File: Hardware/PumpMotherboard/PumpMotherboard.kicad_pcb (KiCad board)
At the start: 2 copper layers, 86.4 x 91.4 mm, 0 parts

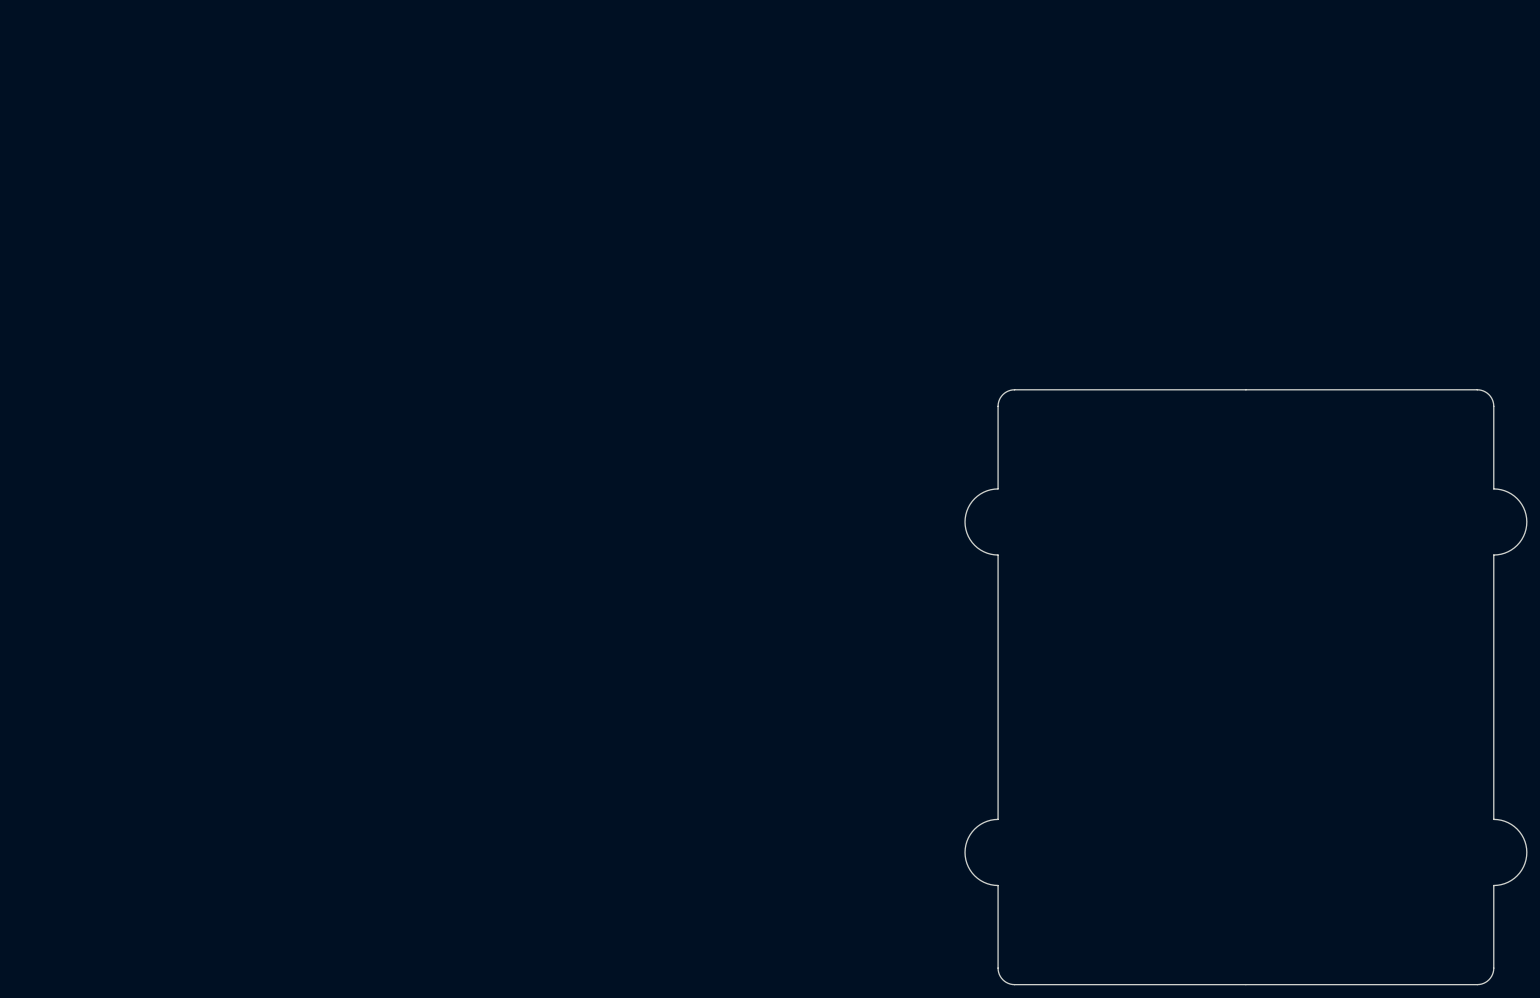
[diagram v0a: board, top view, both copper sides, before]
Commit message: Add more bits to motherboard/controller panel
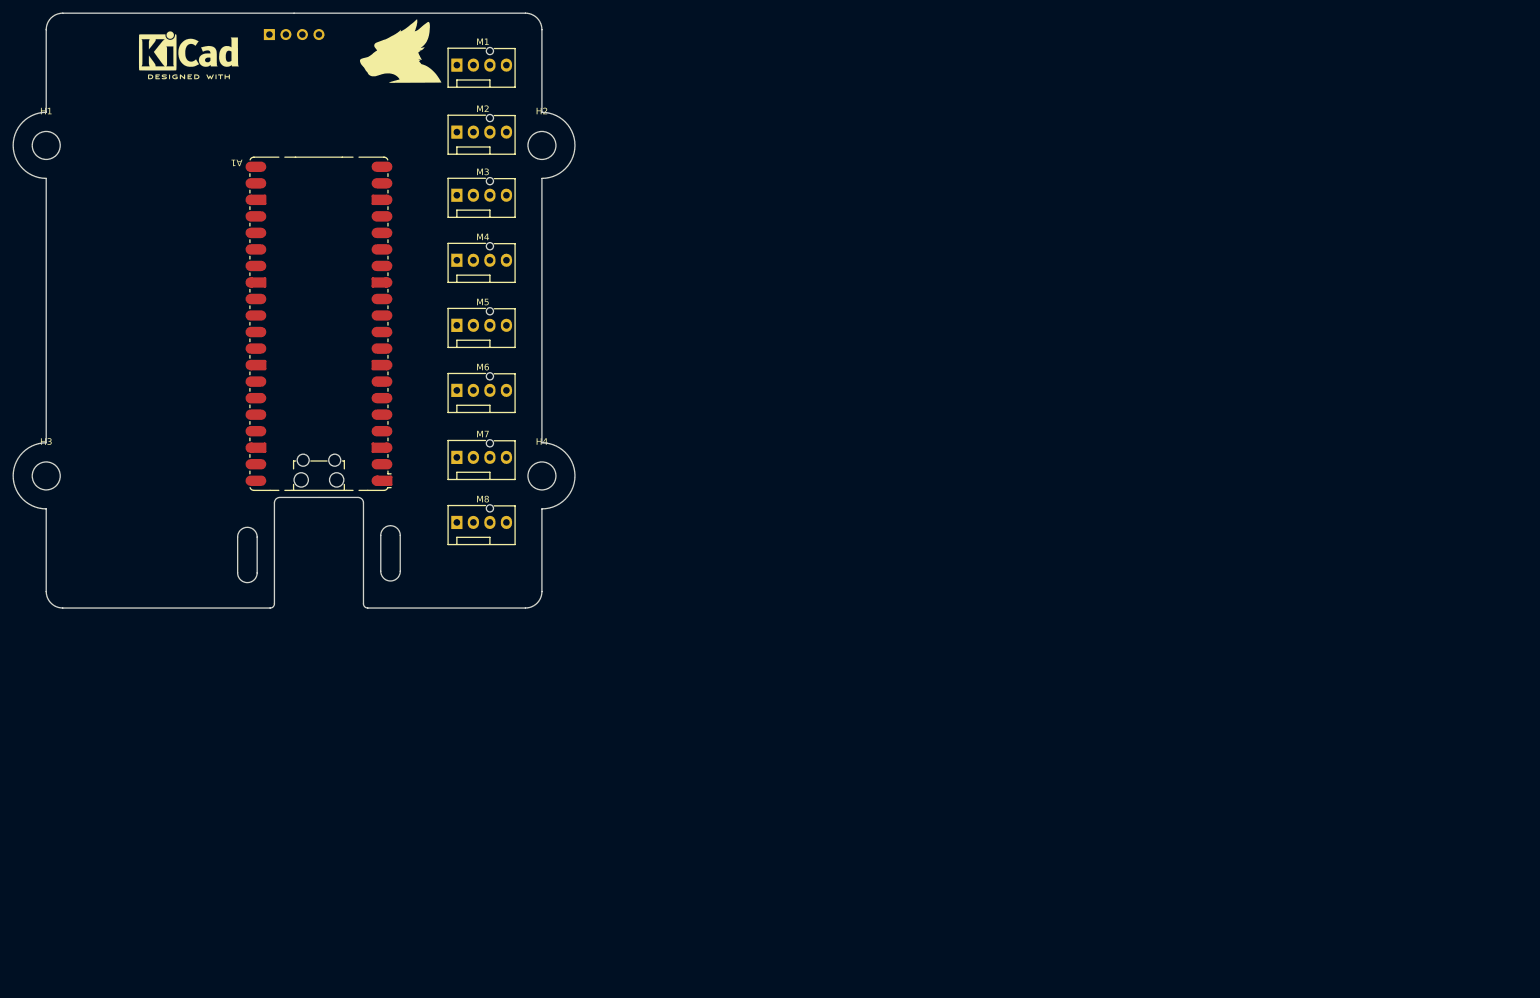
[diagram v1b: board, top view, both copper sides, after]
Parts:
- added A1: RaspberryPi_Pico, Module:RaspberryPi_Pico_Common_SMD, F.Cu at (0.00, 44.5)
- added G***: LOGO, KenwoodFox:KITSUNE_LOGO, F.Cu at (12.5, 2.50)
- added H1: MountingHole, MountingHole:MountingHole_4.3mm_M4, F.Cu at (-41.9, 17.1)
- added H2: MountingHole, MountingHole:MountingHole_4.3mm_M4, F.Cu at (34.3, 17.1)
- added H3: MountingHole, MountingHole:MountingHole_4.3mm_M4, F.Cu at (-41.9, 67.8)
- added H4: MountingHole, MountingHole:MountingHole_4.3mm_M4, F.Cu at (34.3, 67.8)
- added J1: Conn_01x04_Socket, Connector_PinSocket_2.54mm:PinSocket_1x04_P2.54mm_Vertical, B.Cu at (-7.62, 0.00)
- added M1: Fan_4pin, Connector:FanPinHeader_1x04_P2.54mm_Vertical, F.Cu at (21.2, 4.70)
- added M2: Fan_4pin, Connector:FanPinHeader_1x04_P2.54mm_Vertical, F.Cu at (21.2, 15.0)
- added M3: Fan_4pin, Connector:FanPinHeader_1x04_P2.54mm_Vertical, F.Cu at (21.2, 24.7)
- added M4: Fan_4pin, Connector:FanPinHeader_1x04_P2.54mm_Vertical, F.Cu at (21.2, 34.7)
- added M5: Fan_4pin, Connector:FanPinHeader_1x04_P2.54mm_Vertical, F.Cu at (21.2, 44.7)
- added M6: Fan_4pin, Connector:FanPinHeader_1x04_P2.54mm_Vertical, F.Cu at (21.2, 54.7)
- added M7: Fan_4pin, Connector:FanPinHeader_1x04_P2.54mm_Vertical, F.Cu at (21.2, 65.0)
- added M8: Fan_4pin, Connector:FanPinHeader_1x04_P2.54mm_Vertical, F.Cu at (21.2, 75.0)
- added REF**: KiCad-Logo2_6mm_SilkScreen, Symbol:KiCad-Logo2_6mm_SilkScreen, F.Cu at (-20.0, 2.50)
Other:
- outline, holes or cut-outs redrawn

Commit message: Replicate plugin is being a pain
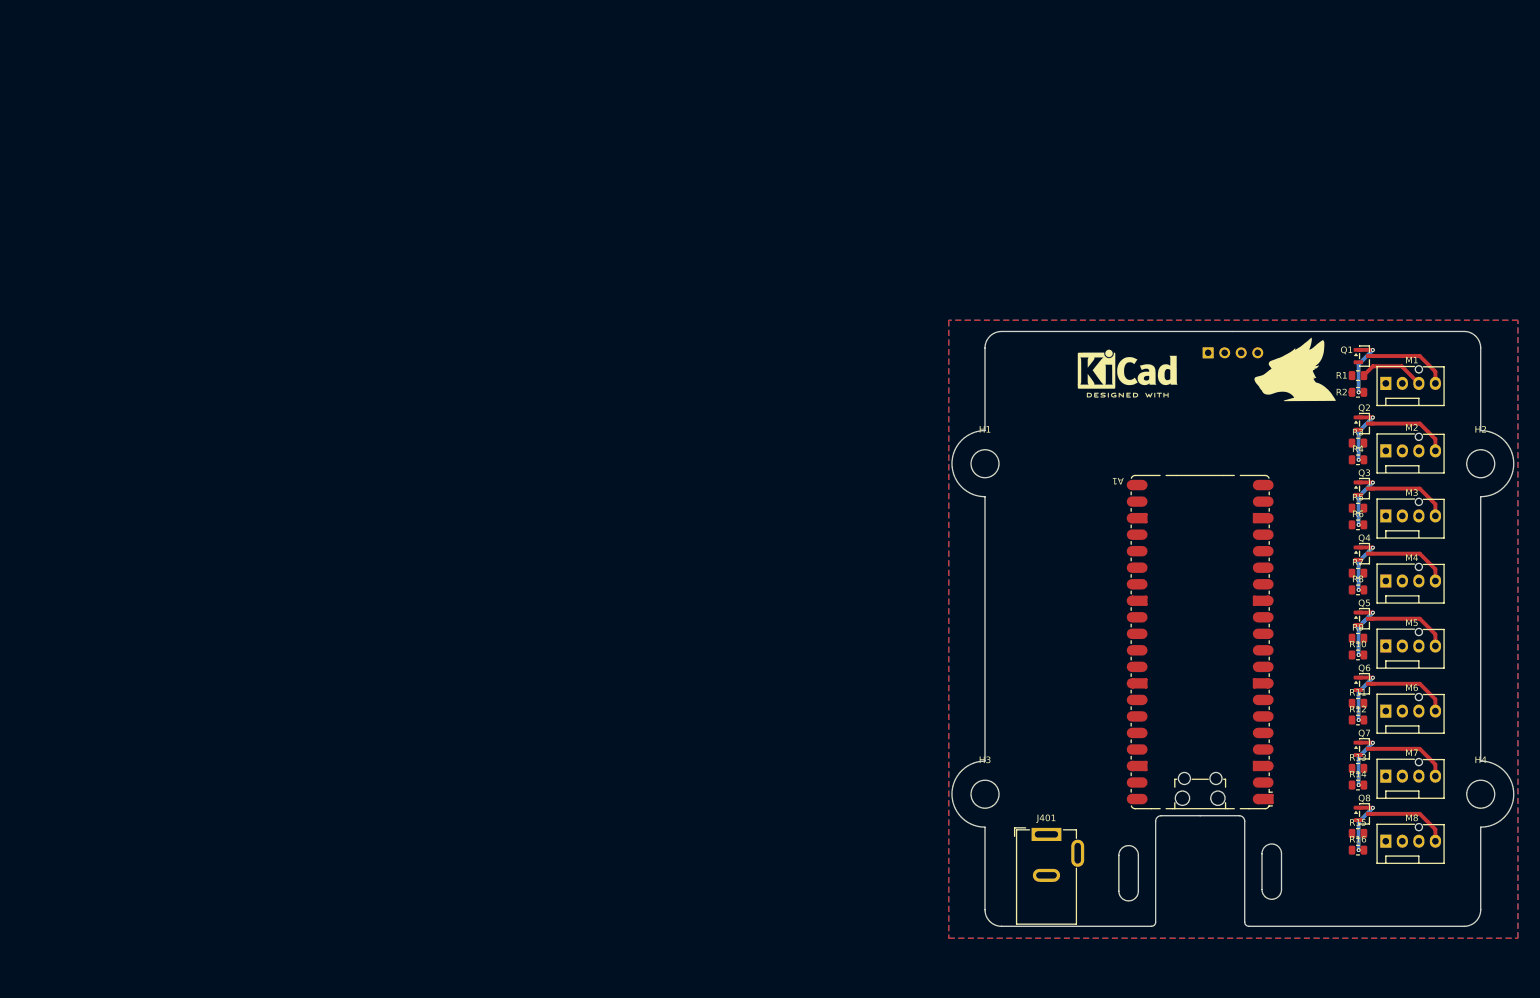
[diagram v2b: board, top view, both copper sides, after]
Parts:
- added J401: 12V Input, Connector_BarrelJack:BarrelJack_GCT_DCJ200-10-A_Horizontal, F.Cu at (111.8, 123.0)
- added Q1: MMBT3904, Package_TO_SOT_SMD:SOT-23, F.Cu at (160.7, 49.4)
- added Q2: MMBT3904, Package_TO_SOT_SMD:SOT-23, F.Cu at (160.7, 59.8)
- added Q3: MMBT3904, Package_TO_SOT_SMD:SOT-23, F.Cu at (160.7, 69.8)
- added Q4: MMBT3904, Package_TO_SOT_SMD:SOT-23, F.Cu at (160.7, 79.8)
- added Q5: MMBT3904, Package_TO_SOT_SMD:SOT-23, F.Cu at (160.7, 89.8)
- added Q6: MMBT3904, Package_TO_SOT_SMD:SOT-23, F.Cu at (160.7, 99.8)
- added Q7: MMBT3904, Package_TO_SOT_SMD:SOT-23, F.Cu at (160.7, 109.8)
- added Q8: MMBT3904, Package_TO_SOT_SMD:SOT-23, F.Cu at (160.7, 119.8)
- added R1: 10K, Resistor_SMD:R_0805_2012Metric, F.Cu at (159.7, 52.4)
- added R10: 10K, Resistor_SMD:R_0805_2012Metric, F.Cu at (159.7, 95.4)
- added R11: 1K, Resistor_SMD:R_0805_2012Metric, F.Cu at (159.7, 102.8)
- added R12: 10K, Resistor_SMD:R_0805_2012Metric, F.Cu at (159.7, 105.4)
- added R13: 1K, Resistor_SMD:R_0805_2012Metric, F.Cu at (159.7, 112.8)
- added R14: 10K, Resistor_SMD:R_0805_2012Metric, F.Cu at (159.7, 115.4)
- added R15: 1K, Resistor_SMD:R_0805_2012Metric, F.Cu at (159.7, 122.8)
- added R16: 10K, Resistor_SMD:R_0805_2012Metric, F.Cu at (159.7, 125.4)
- added R2: 1K, Resistor_SMD:R_0805_2012Metric, F.Cu at (159.7, 55.0)
- added R3: 1K, Resistor_SMD:R_0805_2012Metric, F.Cu at (159.7, 62.8)
- added R4: 10K, Resistor_SMD:R_0805_2012Metric, F.Cu at (159.7, 65.4)
- added R5: 1K, Resistor_SMD:R_0805_2012Metric, F.Cu at (159.7, 72.8)
- added R6: 10K, Resistor_SMD:R_0805_2012Metric, F.Cu at (159.7, 75.4)
- added R7: 1K, Resistor_SMD:R_0805_2012Metric, F.Cu at (159.7, 82.8)
- added R8: 10K, Resistor_SMD:R_0805_2012Metric, F.Cu at (159.7, 85.4)
- added R9: 1K, Resistor_SMD:R_0805_2012Metric, F.Cu at (159.7, 92.8)
- J1: value Conn_01x04_Socket -> BTB
- moved H1 152.4 mm to (102.4, 66.0)
- moved H2 152.4 mm to (178.6, 66.0)
- moved H3 152.4 mm to (102.4, 116.8)
- moved H4 152.4 mm to (178.6, 116.8)
- moved J1 152.4 mm to (136.7, 48.9)
- moved REF** 152.4 mm to (124.3, 51.4)
- moved M3 151.1 mm to (164.0, 74.0)
- moved M4 151.1 mm to (164.0, 84.0)
- moved M5 151.1 mm to (164.0, 94.0)
- moved M6 151.1 mm to (164.0, 104.0)
- moved M2 151.0 mm to (164.0, 64.0)
- moved M7 151.0 mm to (164.0, 114.0)
- moved M8 151.0 mm to (164.0, 124.0)
- moved M1 150.9 mm to (164.0, 53.6)
- moved G*** 145.9 mm to (150.0, 51.4)
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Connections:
- A1 pad 1: unconnected-(A1-GPIO0-Pad1) -> /PWM_7
- A1 pad 10: unconnected-(A1-GPIO7-Pad10) -> /TACH_4
- A1 pad 11: unconnected-(A1-GPIO8-Pad11) -> /PWM_3
- A1 pad 12: unconnected-(A1-GPIO9-Pad12) -> /TACH_3
- A1 pad 13: Net-(A1-GND-Pad13) -> GND
- A1 pad 14: unconnected-(A1-GPIO10-Pad14) -> /PWM_2
- A1 pad 15: unconnected-(A1-GPIO11-Pad15) -> /TACH_2
- A1 pad 16: unconnected-(A1-GPIO12-Pad16) -> /PWM_1
- A1 pad 17: unconnected-(A1-GPIO13-Pad17) -> /TACH_1
- A1 pad 18: Net-(A1-GND-Pad13) -> GND
- A1 pad 19: unconnected-(A1-GPIO14-Pad19) -> /PWM_0
- A1 pad 2: unconnected-(A1-GPIO1-Pad2) -> /TACH_7
- A1 pad 20: unconnected-(A1-GPIO15-Pad20) -> /TACH_0
- A1 pad 23: Net-(A1-GND-Pad13) -> GND
- A1 pad 28: Net-(A1-GND-Pad13) -> GND
- A1 pad 3: Net-(A1-GND-Pad13) -> GND
- A1 pad 33: unconnected-(A1-AGND-Pad33) -> GND
- A1 pad 38: Net-(A1-GND-Pad13) -> GND
- A1 pad 4: unconnected-(A1-GPIO2-Pad4) -> /PWM_6
- A1 pad 5: unconnected-(A1-GPIO3-Pad5) -> /TACH_6
- A1 pad 6: unconnected-(A1-GPIO4-Pad6) -> /PWM_5
- A1 pad 7: unconnected-(A1-GPIO5-Pad7) -> /TACH_5
- A1 pad 8: Net-(A1-GND-Pad13) -> GND
- A1 pad 9: unconnected-(A1-GPIO6-Pad9) -> /PWM_4
- J1 pad 1: unconnected-(J1-Pin_1-Pad1) -> GND
- J1 pad 2: unconnected-(J1-Pin_2-Pad2) -> /NEOPIXEL
- J1 pad 4: unconnected-(J1-Pin_4-Pad4) -> +5V
- M1 pad 3: /M1_TACH -> /TACH_0
- M1 pad 4: /M1_PWM -> Net-(M1-PWM)
- M2 pad 3: /M1_TACH -> /TACH_1
- M2 pad 4: /M1_PWM -> Net-(M2-PWM)
- M3 pad 3: /M1_TACH -> /TACH_2
- M3 pad 4: /M1_PWM -> Net-(M3-PWM)
- M4 pad 3: /M1_TACH -> /TACH_3
- M4 pad 4: /M1_PWM -> Net-(M4-PWM)
- M5 pad 3: /M1_TACH -> /TACH_4
- M5 pad 4: /M1_PWM -> Net-(M5-PWM)
- M6 pad 3: /M1_TACH -> /TACH_5
- M6 pad 4: /M1_PWM -> Net-(M6-PWM)
- M7 pad 3: /M1_TACH -> /TACH_6
- M7 pad 4: /M1_PWM -> Net-(M7-PWM)
- M8 pad 3: /M1_TACH -> /TACH_7
- M8 pad 4: /M1_PWM -> Net-(M8-PWM)
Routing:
- net Net-(Q1-B): track 0.00 -> 83.5 mm, vias 0 -> 16
- net Net-(M8-PWM): track 0.00 -> 12.8 mm
- net Net-(M7-PWM): track 0.00 -> 12.8 mm
- net Net-(M6-PWM): track 0.00 -> 12.8 mm
- net Net-(M5-PWM): track 0.00 -> 12.8 mm
- net Net-(M4-PWM): track 0.00 -> 12.8 mm
- net Net-(M3-PWM): track 0.00 -> 12.8 mm
- net Net-(M2-PWM): track 0.00 -> 12.8 mm
- net Net-(M1-PWM): track 0.00 -> 12.8 mm
- net /TACH_0: track 0.00 -> 10.2 mm
- added copper zone on B.Cu, net +12V
- added copper zone on F.Cu, net GND
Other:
- outline, holes or cut-outs redrawn

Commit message: Add tsensors, misc bits
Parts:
- added C1: 10uF, Capacitor_SMD:CP_Elec_4x3, F.Cu at (116.8, 117.0)
- added C2: 100nF, Capacitor_SMD:C_0805_2012Metric, F.Cu at (109.4, 110.0)
- added D1: PWR, LED_SMD:LED_0805_2012Metric, F.Cu at (112.9, 65.6)
- added J2: Conn_01x03_Pin, Connector_JST:JST_PH_B3B-PH-K_1x03_P2.00mm_Vertical, F.Cu at (118.0, 74.0)
- added J3: T_SENSOR, Connector_PinHeader_2.54mm:PinHeader_1x02_P2.54mm_Vertical, F.Cu at (116.5, 86.5)
- added J4: T_SENSOR, Connector_PinHeader_2.54mm:PinHeader_1x02_P2.54mm_Vertical, F.Cu at (116.5, 92.9)
- added J5: T_SENSOR, Connector_PinHeader_2.54mm:PinHeader_1x02_P2.54mm_Vertical, F.Cu at (116.5, 99.3)
- added L1: 4.7uH, Inductor_SMD:L_APV_ANR4012, F.Cu at (112.8, 107.6)
- added R17: 0R, Resistor_SMD:R_0805_2012Metric, F.Cu at (128.8, 61.6)
- added R18: 1K, Resistor_SMD:R_0805_2012Metric, F.Cu at (112.9, 63.2)
- added R19: 10K, Resistor_SMD:R_0805_2012Metric, F.Cu at (120.1, 89.0)
- added R20: 10K, Resistor_SMD:R_0805_2012Metric, F.Cu at (120.1, 95.4)
- added R21: 10K, Resistor_SMD:R_0805_2012Metric, F.Cu at (120.1, 101.7)
- added U2: AP63205WU, Package_TO_SOT_SMD:TSOT-23-6, F.Cu at (112.8, 112.4)
- moved R16 70.0 mm to (130.8, 61.6), turned to -90 degrees
- moved R14 60.1 mm to (132.8, 61.6), turned to -90 degrees
- moved R12 50.4 mm to (134.8, 61.6), turned to -90 degrees
- moved R10 40.8 mm to (136.8, 61.6), turned to -90 degrees
- moved R8 31.7 mm to (138.8, 61.6), turned to -90 degrees
- moved R6 23.4 mm to (140.8, 61.6), turned to -90 degrees
- moved R1 17.5 mm to (144.8, 61.6), turned to -90 degrees
- moved R4 17.3 mm to (142.8, 61.6), turned to -90 degrees
- moved R11 2.60 mm to (159.7, 105.4)
- moved R13 2.60 mm to (159.7, 115.4)
- moved R15 2.60 mm to (159.7, 125.4)
- moved R3 2.60 mm to (159.7, 65.4)
- moved R5 2.60 mm to (159.7, 75.4)
- moved R7 2.60 mm to (159.7, 85.4)
- moved R9 2.60 mm to (159.7, 95.4)
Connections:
- A1 pad 21: unconnected-(A1-GPIO16-Pad21) -> Net-(A1-GPIO16)
- A1 pad 22: unconnected-(A1-GPIO17-Pad22) -> /AC_LEDS
- A1 pad 31: unconnected-(A1-GPIO26_ADC0-Pad31) -> /TSENSOR_0
- A1 pad 32: unconnected-(A1-GPIO27_ADC1-Pad32) -> /TSENSOR_1
- A1 pad 34: unconnected-(A1-GPIO28_ADC2-Pad34) -> /TSENSOR_2
- A1 pad 36: unconnected-(A1-3V3-Pad36) -> +3V3
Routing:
- net +12V: track 0.00 -> 149.7 mm
- net +5V: track 0.00 -> 123.7 mm, vias 0 -> 3
- net /TACH_7: track 0.00 -> 90.8 mm
- net +3V3: track 0.00 -> 88.1 mm, vias 0 -> 5
- net /TACH_6: track 0.00 -> 80.7 mm
- net /TACH_5: track 0.00 -> 73.9 mm
- net Net-(Q1-B): track 83.5 -> 10.4 mm, vias 16 -> 2
- net /TACH_4: track 0.00 -> 63.8 mm
- net /TACH_3: track 0.00 -> 60.3 mm
- net /TACH_2: track 0.00 -> 50.3 mm
- net /TACH_1: track 0.00 -> 48.4 mm
- net /TACH_0: track 10.2 -> 42.7 mm
- net /PWM_0: track 0.31 -> 23.8 mm
- net /PWM_1: track 0.00 -> 21.5 mm
- net /NEOPIXEL: track 0.00 -> 17.5 mm
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- added copper zone on B.Cu, net GND
- removed copper zone on B.Cu, net +12V
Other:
- board text added: "AC_LED"
- board text added: "Designed in New Hampshire By Joe 2026"
- board text added: "Rack Cooler Controller ${FULL_REVISION}"
- board text added: "T0"
- board text added: "T1"
- board text added: "T2"

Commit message: Fix DRC and ERC and add AGND
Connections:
- A1 pad 33: GND -> GNDA
- A1 pad 39: unconnected-(A1-VSYS-Pad39) -> +5V
- J3 pad 1: GND -> GNDA
- J4 pad 1: GND -> GNDA
- J5 pad 1: GND -> GNDA
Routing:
- net /TACH_1: track 48.4 -> 49.0 mm
- added copper zone on F.Cu, net GNDA

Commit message: Add SW inputs
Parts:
- added J6: SW_IN0, Connector_JST:JST_XH_B2B-XH-A_1x02_P2.50mm_Vertical, F.Cu at (120.0, 72.0)
- added J7: SW_IN1, Connector_JST:JST_XH_B2B-XH-A_1x02_P2.50mm_Vertical, F.Cu at (120.0, 79.0)
- added J8: SW_IN2, Connector_JST:JST_XH_B2B-XH-A_1x02_P2.50mm_Vertical, F.Cu at (109.0, 79.0)
- J2: value Conn_01x03_Pin -> AC_LEDs; footprint Connector_JST:JST_PH_B3B-PH-K_1x03_P2.00mm_Vertical -> Connector_JST:JST_XH_B3B-XH-A_1x03_P2.50mm_Vertical
- moved J2 12.3 mm to (124.5, 63.5), turned to 180 degrees
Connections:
- A1 pad 24: unconnected-(A1-GPIO18-Pad24) -> /SW_0
- A1 pad 25: unconnected-(A1-GPIO19-Pad25) -> /SW_1
- A1 pad 26: unconnected-(A1-GPIO20-Pad26) -> /SW_2
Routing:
- net /SW_2: track 0.00 -> 18.0 mm, vias 0 -> 1
- net /SW_0: track 0.00 -> 7.80 mm
- net /SW_1: track 0.00 -> 5.95 mm
- net +5V: track 123.7 -> 118.0 mm
- net /AC_LEDS: track 7.81 -> 10.7 mm
- net GND: vias 33 -> 32
